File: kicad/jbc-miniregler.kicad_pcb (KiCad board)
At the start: 2 copper layers, 97 x 111 mm, 110 parts, among them J1 Power IN, J2 COM, J3 Lötkolben, Q1 KND3508A, Q2 2N7002, Q3 MMBT3904, Q4 MMBT3904, Q5 ZXMP10A13FTA, SW1 UP, SW2 DOWN, SW3 ENTER, SW4 BACK, SW5 Ein/Aus, U1 OLED-128x32-Module, U2 74LVC1G125, U3 NST175, U4 GS8332-SR, U5 PN7006A, U6 XL7005A, U7 XL7005A, U8 MAX3232

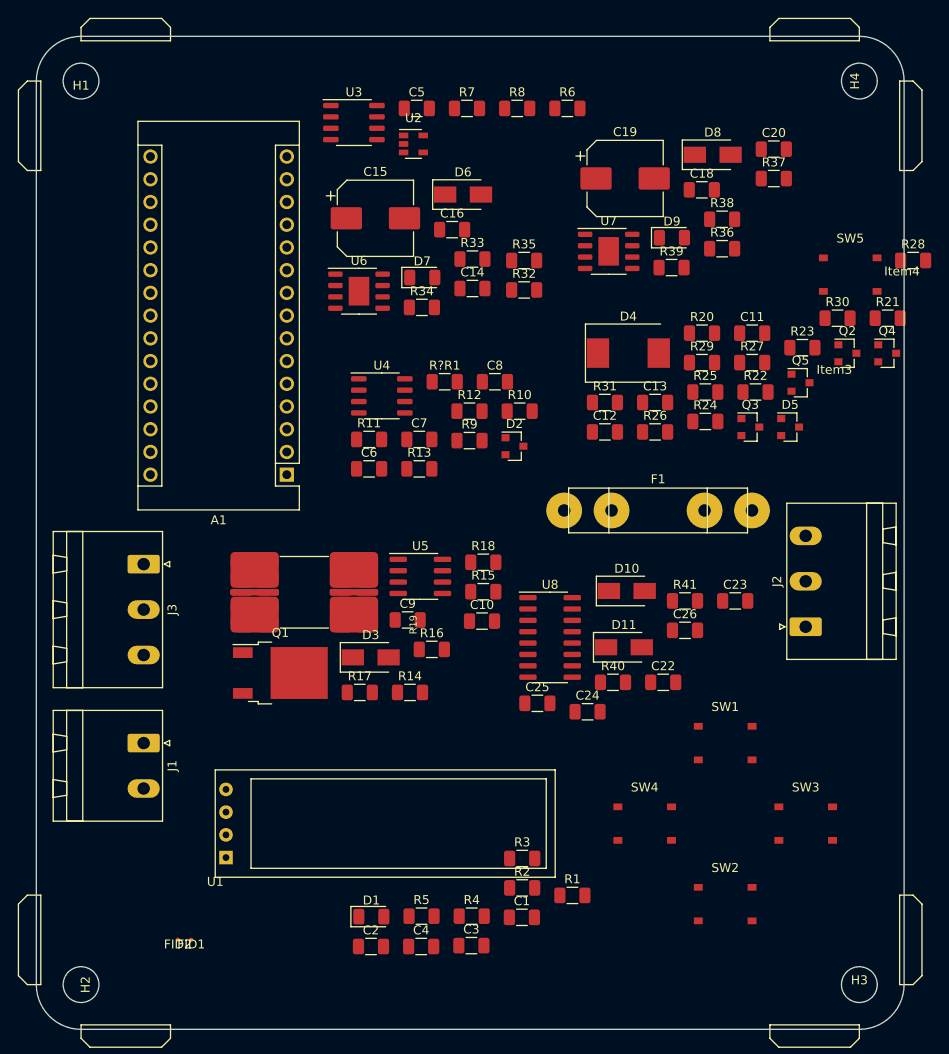
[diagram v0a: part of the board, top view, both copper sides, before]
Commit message: BOM Fertig, 3D auch fast fertig. Ein paar Footrpints fehlen noch.
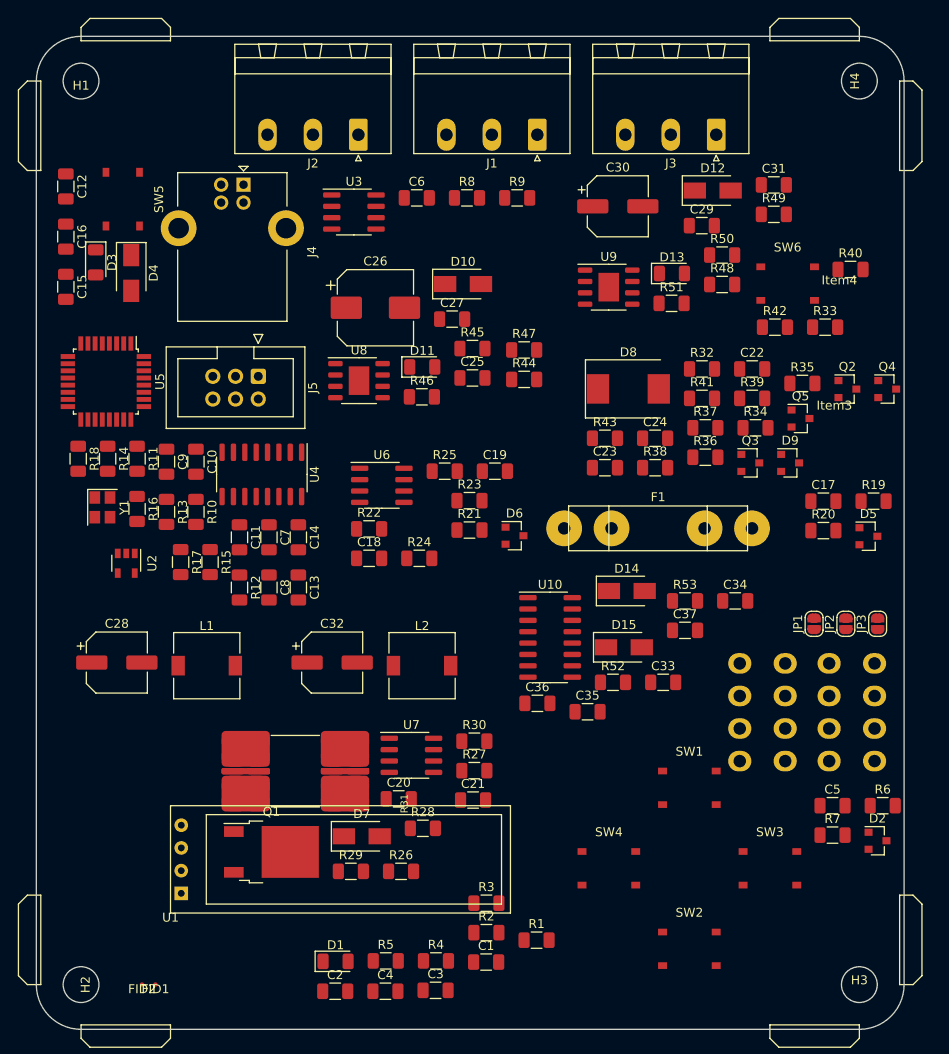
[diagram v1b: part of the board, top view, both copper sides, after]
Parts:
- removed A1: Arduino_Nano_v3.x, Module:Arduino_Nano
- removed the C19 at (103.8, 40.9)
- added C10: 1u, Capacitor_SMD:C_1206_3216Metric, F.Cu at (55.8, 72.5)
- added C11: 100n, Capacitor_SMD:C_1206_3216Metric, F.Cu at (60.7, 81.0)
- added C12: 1u, Capacitor_SMD:C_1206_3216Metric, F.Cu at (41.3, 41.8)
- added C13: 1u, Capacitor_SMD:C_1206_3216Metric, F.Cu at (67.3, 86.6)
- added C14: 100n, Capacitor_SMD:C_1206_3216Metric, F.Cu at (67.3, 81.0)
- added C15: 12p, Capacitor_SMD:C_1206_3216Metric, F.Cu at (41.3, 53.0)
- added C16: 12p, Capacitor_SMD:C_1206_3216Metric, F.Cu at (41.3, 47.4)
- added C17: 100n, Capacitor_SMD:C_1206_3216Metric, F.Cu at (126.0, 77.0)
- added C28: 100u/25V, Capacitor_SMD:CP_Elec_6.3x5.9, F.Cu at (47.0, 95.0)
- added C30: 100u/25V, Capacitor_SMD:CP_Elec_6.3x5.9, F.Cu at (103.0, 44.0)
- added C32: 100u/25V, Capacitor_SMD:CP_Elec_6.3x5.9, F.Cu at (71.1, 95.0)
- added C5: 100n, Capacitor_SMD:C_1206_3216Metric, F.Cu at (127.0, 111.0)
- added C8: 100n, Capacitor_SMD:C_1206_3216Metric, F.Cu at (64.0, 86.6)
- added C9: 100n, Capacitor_SMD:C_1206_3216Metric, F.Cu at (52.5, 72.5)
- added D2: BAV99, Package_TO_SOT_SMD:SOT-23, F.Cu at (132.0, 114.9)
- added D3: grün, LED_SMD:LED_1206_3216Metric, F.Cu at (44.6, 50.3)
- added D4: SS210, Diode_SMD:D_SMA, F.Cu at (48.6, 51.5)
- added D5: BAV99, Package_TO_SOT_SMD:SOT-23, F.Cu at (131.0, 80.9)
- added J10: Makita Minus, htl_connectors:Faston_Tab_6.3mm_vertical, B.Cu at (116.6, 102.4)
- added J11: Bosch Minus, htl_connectors:Faston_Tab_6.3mm_vertical, B.Cu at (126.6, 106.0)
- added J12: ActivEnergy B2-, htl_connectors:Faston_Tab_6.3mm_vertical, B.Cu at (116.6, 98.7)
- added J13: ActivEnergy B1-, htl_connectors:Faston_Tab_6.3mm_vertical, B.Cu at (126.6, 102.4)
- added J4: USB_B, Connector_USB:USB_B_Lumberg_2411_02_Horizontal, F.Cu at (61.2, 41.6)
- added J5: AVR ISP, Connector_IDC:IDC-Header_2x03_P2.54mm_Vertical, F.Cu at (62.8, 63.0)
- added J6: ActivEnergy B2+, htl_connectors:Faston_Tab_6.3mm_vertical, B.Cu at (126.6, 95.1)
- added J7: ActivEnergy B1+, htl_connectors:Faston_Tab_6.3mm_vertical, B.Cu at (126.6, 98.7)
- added J8: Makita Plus, htl_connectors:Faston_Tab_6.3mm_vertical, B.Cu at (116.6, 95.1)
- added J9: Bosch Plus, htl_connectors:Faston_Tab_6.3mm_vertical, B.Cu at (116.6, 106.0)
- added JP1: 20V, Jumper:SolderJumper-2_P1.3mm_Open_RoundedPad1.0x1.5mm, F.Cu at (124.9, 90.7)
- added JP2: 40V, Jumper:SolderJumper-2_P1.3mm_Open_RoundedPad1.0x1.5mm, F.Cu at (128.5, 90.7)
- added JP3: 20V, Jumper:SolderJumper-2_P1.3mm_Open_RoundedPad1.0x1.5mm, F.Cu at (132.0, 90.7)
- added L1: 47u/1A, Inductor_SMD:L_7.3x7.3_H4.5, F.Cu at (57.0, 95.3)
- added L2: 47u/1A, Inductor_SMD:L_7.3x7.3_H4.5, F.Cu at (81.1, 95.3)
- added R11: 1k, Resistor_SMD:R_1206_3216Metric, F.Cu at (49.3, 72.2)
- added R12: 100R, Resistor_SMD:R_1206_3216Metric, F.Cu at (60.7, 86.6)
- added R13: 1k, Resistor_SMD:R_1206_3216Metric, F.Cu at (52.5, 78.2)
- added R14: 100R, Resistor_SMD:R_1206_3216Metric, F.Cu at (46.0, 72.2)
- added R15: 100R, Resistor_SMD:R_1206_3216Metric, F.Cu at (57.4, 83.8)
- added R16: 100R, Resistor_SMD:R_1206_3216Metric, F.Cu at (49.3, 77.8)
- added R17: 1k, Resistor_SMD:R_1206_3216Metric, F.Cu at (54.1, 83.8)
- added R18: 100R, Resistor_SMD:R_1206_3216Metric, F.Cu at (42.7, 72.2)
- added R19: 100k, Resistor_SMD:R_1206_3216Metric, F.Cu at (131.6, 77.0)
- added R20: 1k, Resistor_SMD:R_1206_3216Metric, F.Cu at (126.0, 80.2)
- added R7: 10k, Resistor_SMD:R_1206_3216Metric, F.Cu at (127.0, 114.3)
- added SW5: Reset, htl_smd:SW_Push_5.1mm_H1.5mm, F.Cu at (47.7, 43.2)
- added U4: CH340C, Package_SO:SOIC-16_3.9x9.9mm_P1.27mm, F.Cu at (63.2, 74.0)
- added U5: ATmega328P-AU, Package_QFP:TQFP-32_7x7mm_P0.8mm, F.Cu at (45.8, 63.6)
- added Y1: 16MHz, Crystal:Crystal_SMD_3225-4Pin_3.2x2.5mm, F.Cu at (45.4, 77.7)
- C7: value 10n -> 1u
- Item2: value PCB, 2 Layer, 35um Cu, 1.6mm, TODO size -> PCB, 1 Layer, 35um Cu, 1.6mm, ca. 100x110
- J1: value Power IN -> COM; footprint Connector_Phoenix_MSTB:PhoenixContact_MSTBA_2,5_2-G-5,08_1x02_P5.08mm_Horizontal -> Connector_Phoenix_MSTB:PhoenixContact_MSTBA_2,5_3-G-5,08_1x03_P5.08mm_Horizontal
- U3: footprint Package_SO:SO-8_3.9x4.9mm_P1.27mm -> Package_SO:SOIC-8_3.9x4.9mm_P1.27mm
- U6: renamed from U4; footprint Package_SO:SO-8_3.9x4.9mm_P1.27mm -> Package_SO:SOIC-8_3.9x4.9mm_P1.27mm
- moved R6 85.5 mm to (132.6, 111.0)
- moved J1 81.0 mm to (94.0, 36.0), turned to 180 degrees
- moved J3 80.0 mm to (114.0, 36.0), turned to 180 degrees
- moved J2 74.3 mm to (74.0, 36.0), turned to 180 degrees
- moved U2 56.8 mm to (48.0, 83.9), turned to 270 degrees
- moved R10 37.9 mm to (55.8, 78.2), turned to 270 degrees
- moved C7 20.1 mm to (64.0, 81.0), turned to 270 degrees
- moved C20 20.0 mm to (78.5, 110.2)
- moved C21 20.0 mm to (86.8, 110.4)
- moved D7 20.0 mm to (74.4, 114.4)
- moved Q1 20.0 mm to (64.3, 116.2)
- moved R26 20.0 mm to (78.8, 118.3)
- moved R27 20.0 mm to (87.0, 107.1)
- moved R28 20.0 mm to (81.2, 113.5)
- moved R29 20.0 mm to (73.2, 118.3)
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- renumbered C6 to C18, C8 to C19, C9 to C20, C10 to C21, C11 to C22, C12 to C23, C13 to C24, C14 to C25, C15 to C26, C16 to C27, C18 to C29, C20 to C31, C22 to C33, C23 to C34, C24 to C35, C25 to C36, C26 to C37, C5 to C6, D6 to D10, D7 to D11, D8 to D12, D9 to D13, D10 to D14, D11 to D15, D2 to D6, D3 to D7, D4 to D8, D5 to D9, R9 to R21, R11 to R22, R12 to R23, R13 to R24, R?R1 to R25, R14 to R26, R15 to R27, R16 to R28, R17 to R29, R18 to R30, R19 to R31, R20 to R32, R21 to R33, R22 to R34, R23 to R35, R24 to R36, R25 to R37, R26 to R38, R27 to R39, R28 to R40, R29 to R41, R30 to R42, R31 to R43, R32 to R44, R33 to R45, R34 to R46, R35 to R47, R36 to R48, R37 to R49, R38 to R50, R39 to R51, R40 to R52, R41 to R53, R7 to R8, R8 to R9, SW5 to SW6, U8 to U10, U5 to U7, U6 to U8, U7 to U9
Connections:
- C7 pad 1: Net-(C7-Pad1) -> /Arduino/VUSB
- R10 pad 1: Net-(C7-Pad1) -> /Arduino/VUSB
- R10 pad 2: /Messverstärker/Shunt -> Net-(D3-Pad2)
- R6 pad 1: +5V -> /Arduino/Lötkolbenständer
- R6 pad 2: /Arduino/~RS232-Rx-Enable -> /Arduino/Arduino Nano/A6
- U1 pad 2: (no net) -> +5V
- U2 pad 1: /Arduino/~RS232-Rx-Enable -> /Arduino/VUSB
- U2 pad 4: Net-(A1-Pad2) -> /Arduino/Arduino Nano/D0_RX
- U6 pad 5: Net-(C7-Pad1) -> Net-(C17-Pad2)

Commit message: Reviews und ein paar Verbesserungen
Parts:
- removed J1: COM, Connector_Phoenix_MSTB:PhoenixContact_MSTBA_2,5_3-G-5,08_1x03_P5.08mm_Horizontal
- added C38: 10n, Capacitor_SMD:C_1206_3216Metric, F.Cu at (42.4, 83.1)
- added X1: POWER, htl_connectors:Federklemme_KF142_3P_P5.08mm_C475145, F.Cu at (97.0, 37.6)
- J4: footprint Connector_USB:USB_B_Lumberg_2411_02_Horizontal -> htl_connectors:USB_B_Lumberg_2411_02_Horizontal
- R37: value 100k -> 10k
- X2: renamed from J2; footprint Connector_Phoenix_MSTB:PhoenixContact_MSTBA_2,5_3-G-5,08_1x03_P5.08mm_Horizontal -> htl_connectors:Federklemme_KF142_3P_P5.08mm_C475145
- X3: renamed from J3; footprint Connector_Phoenix_MSTB:PhoenixContact_MSTBA_2,5_3-G-5,08_1x03_P5.08mm_Horizontal -> htl_connectors:Federklemme_KF142_3P_P5.08mm_C475145
- moved C15 17.7 mm to (59.0, 53.7), turned to 0 degrees
- moved C16 13.6 mm to (53.4, 53.7), turned to 0 degrees
- moved C12 13.6 mm to (47.8, 53.7), turned to 0 degrees
- moved D3 11.6 mm to (56.3, 50.4), turned to 0 degrees
- moved D4 10.2 mm to (57.5, 46.4), turned to 0 degrees
- moved J4 8.31 mm to (53.0, 40.0), turned to 90 degrees
- moved SW5 4.42 mm to (49.2, 47.3), turned to 0 degrees
- moved X2 4.32 mm to (78.0, 37.6)
- moved X3 2.57 mm to (116.0, 37.6)

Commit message: Layout
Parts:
- removed H1, H2, H3, H4: MountingHole, htl_mechanical:mountinghole_d4mm_R5mm
- removed J11: Bosch Minus, htl_connectors:Faston_Tab_6.3mm_vertical
- removed J9: Bosch Plus, htl_connectors:Faston_Tab_6.3mm_vertical
- added C39: 100n, Capacitor_SMD:C_1206_3216Metric, F.Cu at (214.5, 33.0)
- added J1: Makita Plus, htl_connectors:Faston_Tab_6.3mm_vertical, B.Cu at (112.5, 112.5)
- added J2: Makita Minus, htl_connectors:Faston_Tab_6.3mm_vertical, B.Cu at (112.5, 73.5)
- added JP4: UART, Jumper:SolderJumper-3_P2.0mm_Open_TrianglePad1.0x1.5mm_NumberLabels, F.Cu at (215.2, 29.6)
- added JP5: UART, Jumper:SolderJumper-3_P2.0mm_Open_TrianglePad1.0x1.5mm_NumberLabels, F.Cu at (223.6, 23.1)
- added JP6: COM, Jumper:SolderJumper-3_P2.0mm_Open_TrianglePad1.0x1.5mm_NumberLabels, F.Cu at (222.2, 29.6)
- added JP7: COM, Jumper:SolderJumper-3_P2.0mm_Open_TrianglePad1.0x1.5mm_NumberLabels, F.Cu at (230.7, 23.1)
- added R54: 3k3, Resistor_SMD:R_1206_3216Metric, F.Cu at (220.1, 33.0)
- added R55: 1k, Resistor_SMD:R_1206_3216Metric, F.Cu at (228.5, 26.5)
- added R56: 1k, Resistor_SMD:R_1206_3216Metric, F.Cu at (228.5, 29.8)
- added R57: 10R, Resistor_SMD:R_1206_3216Metric, F.Cu at (225.7, 33.1)
- added R58: 10R, Resistor_SMD:R_1206_3216Metric, F.Cu at (231.3, 33.1)
- added U11: YD3082EESA, Package_SO:SO-8_3.9x4.9mm_P1.27mm, F.Cu at (215.9, 24.5)
- moved C12 194.6 mm to (232.5, 115.0)
- moved C15 194.6 mm to (243.8, 115.0)
- moved C16 194.6 mm to (238.1, 115.0)
- moved D3 194.6 mm to (241.0, 111.6)
- moved D4 194.6 mm to (242.2, 107.6)
- moved C10 184.8 mm to (240.6, 71.5)
- moved C11 184.8 mm to (245.5, 80.0)
- moved C13 184.8 mm to (252.0, 85.6)
- moved C14 184.8 mm to (252.0, 80.0)
- moved C38 184.8 mm to (227.2, 82.1)
- moved C7 184.8 mm to (248.8, 80.0)
- moved C8 184.8 mm to (248.8, 85.6)
- moved C9 184.8 mm to (237.3, 71.5)
- moved J5 184.8 mm to (247.6, 62.0)
- moved R10 184.8 mm to (240.6, 77.2)
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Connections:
- R52 pad 1: /UART-RS232/RS232_Tx1 -> Net-(D14-Pad1)
- R52 pad 2: Net-(D14-Pad1) -> Net-(R52-Pad2)
- R53 pad 1: /UART-RS232/RS232_Rx1 -> Net-(D15-Pad1)
- R53 pad 2: Net-(D15-Pad1) -> Net-(R53-Pad2)
- U10 pad 11: /Arduino/TxD -> Net-(JP4-Pad3)
- U10 pad 12: /Arduino/RxD -> Net-(JP5-Pad3)
- U10 pad 13: Net-(D15-Pad1) -> Net-(R53-Pad2)
- U10 pad 14: Net-(D14-Pad1) -> Net-(R52-Pad2)
- U5 pad 13: (no net) -> /Arduino/ComDriverEnable
- X2 pad 1: /UART-RS232/RS232_Rx1 -> /UART RS232/RS485/TxD_A
- X2 pad 2: /UART-RS232/RS232_Tx1 -> /UART RS232/RS485/RxD_B
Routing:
- net /Leistungsteil/H+: track 0.00 -> 26.3 mm, vias 0 -> 17
- net GND: track 0.00 -> 21.7 mm, vias 0 -> 7
- net Net-(C21-Pad1): track 0.00 -> 15.0 mm, vias 0 -> 2
- net Net-(Q1-Pad1): track 0.00 -> 14.6 mm, vias 0 -> 2
- net /Leistungsteil/12V: track 0.00 -> 11.4 mm
- net Net-(R27-Pad1): track 0.00 -> 8.70 mm
- net Net-(R29-Pad2): track 0.00 -> 8.65 mm
- net /Messverstärker/Shunt: track 0.00 -> 7.71 mm
- net /Arduino/Heizelement: track 0.00 -> 7.48 mm
- net Net-(R28-Pad1): track 0.00 -> 5.41 mm
- added copper zone on F.Cu, net +BATT
- added copper zone on B.Cu, net /Leistungsteil/H+
- added copper zone on F.Cu, net /Leistungsteil/H+
- added copper zone on F.Cu, net /Leistungsteil/HTC-
- added copper zone on B.Cu, net /Stromversorgung/BAT+
- added copper zone on F.Cu, net /Stromversorgung/BAT+
- added copper zone on B.Cu, net GNDPWR
- added copper zone on F.Cu, net GNDPWR
- added copper zone on F.Cu, net Net-(J12-Pad1)
- added copper zone on F.Cu, net Net-(J7-Pad1)
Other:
- board size 97 x 111 mm -> 110 x 100 mm
- net class 10A added: clearance 0.25, trace_width 10, via_dia 1, via_drill 0.5
- net class Default: clearance 0.25 -> 0.15; trace_width 0.25 -> 0.15
- rule trace_clearance: 0.25 -> 0.15
- rule trace_min: 0.25 -> 0.15
- rule via_min_size: 0.4 -> 0.6

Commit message: wip
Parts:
- added H1: MountingHole, htl_mechanical:mountinghole_d4mm_R5mm, F.Cu at (25.0, 166.8)
- added H2: MountingHole, htl_mechanical:mountinghole_d4mm_R5mm, F.Cu at (25.0, 185.4)
- added H3: MountingHole, htl_mechanical:mountinghole_d4mm_R5mm, F.Cu at (43.6, 166.8)
- added H4: MountingHole, htl_mechanical:mountinghole_d4mm_R5mm, F.Cu at (43.6, 185.4)
- moved D13 99.7 mm to (99.8, 189.8)
- moved R51 93.9 mm to (105.2, 189.7), turned to 180 degrees
- moved C19 93.7 mm to (84.5, 110.4)
- moved R21 93.7 mm to (81.7, 116.9)
- moved R22 93.7 mm to (70.5, 116.8)
- moved R23 93.7 mm to (81.7, 113.7)
- moved R24 93.7 mm to (76.1, 120.1)
- moved R25 93.7 mm to (78.9, 110.4)
- moved U6 93.7 mm to (71.9, 111.9)
- moved C18 93.7 mm to (70.5, 120.1)
- moved D6 93.7 mm to (86.7, 117.6)
- moved R41 85.4 mm to (144.8, 101.8), turned to 90 degrees
- moved R5 76.5 mm to (153.2, 135.2), turned to 270 degrees
- moved D1 76.1 mm to (153.2, 140.1)
- moved R42 60.8 mm to (158.2, 137.2), turned to 180 degrees
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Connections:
- net Net-(C27-Pad2) renamed /Stromversorgung/Spannungsregler 12V/fb
- net Net-(C31-Pad2) renamed /Stromversorgung/Spannungsregler 5V/fb
- net Net-(D10-Pad1) renamed /Stromversorgung/Spannungsregler 12V/sw
- net Net-(D12-Pad1) renamed /Stromversorgung/Spannungsregler 5V/sw
- net Net-(R44-Pad1) renamed /Stromversorgung/Spannungsregler 12V/~en
- net Net-(R48-Pad1) renamed /Stromversorgung/Spannungsregler 5V/~en
- U8 pad 9: (no net) -> GNDPWR
- U9 pad 9: (no net) -> GNDPWR
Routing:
- net /Leistungsteil/12V: track 11.4 -> 33.2 mm, vias 0 -> 2
- net /Stromversorgung/Spannungsregler 12V/fb: track 0.00 -> 15.1 mm, vias 0 -> 2
- net /Stromversorgung/Spannungsregler 5V/fb: track 0.00 -> 15.0 mm, vias 0 -> 2
- net /Stromversorgung/Spannungsregler 12V/~en: track 0.00 -> 12.5 mm, vias 0 -> 2
- net /Stromversorgung/Spannungsregler 5V/~en: track 0.00 -> 12.2 mm, vias 0 -> 2
- net /Arduino/ENTER: track 0.00 -> 11.0 mm
- net /Arduino/UP: track 0.00 -> 10.9 mm
- net /Arduino/DOWN: track 0.00 -> 10.9 mm
- net /Arduino/BACK: track 0.00 -> 10.4 mm
- net /Arduino/Heizelement: track 7.48 -> 14.5 mm
- net /Messverstärker/Shunt: track 7.71 -> 5.50 mm
- net Net-(D1-Pad2): track 0.00 -> 2.05 mm
- net GND: track 21.7 -> 21.4 mm, vias 7 -> 8
- added copper zone on F.Cu, net /Leistungsteil/12V
- added copper zone on F.Cu, net /Stromversorgung/Spannungsregler 12V/IN
- added copper zone on F.Cu, net /Stromversorgung/Spannungsregler 12V/sw
- added copper zone on F.Cu, net /Stromversorgung/Spannungsregler 5V/5V
- added copper zone on F.Cu, net /Stromversorgung/Spannungsregler 5V/IN
- added copper zone on F.Cu, net /Stromversorgung/Spannungsregler 5V/sw

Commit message: WIP Layout, TODO: DRC
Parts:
- D10, D12, D4, D7: footprint Diode_SMD:D_SMA -> htl_smd:D_SMA_wide
- JP1, JP2, JP3: footprint Jumper:SolderJumper-2_P1.3mm_Open_RoundedPad1.0x1.5mm -> htl_smd:SolderJumper-2_2.2x8mm_Open
- L1, L2: footprint Inductor_SMD:L_7.3x7.3_H4.5 -> htl_smd:L_7.3x7.3_H4.5_C216198
- moved Q2 152.3 mm to (108.0, 59.8)
- moved D9 148.3 mm to (115.2, 59.0), turned to 90 degrees
- moved Q4 145.0 mm to (122.8, 59.0)
- moved R33 143.4 mm to (111.8, 59.2), turned to 270 degrees
- moved Q3 142.6 mm to (119.0, 59.0)
- moved R32 141.3 mm to (104.8, 59.2), turned to 90 degrees
- moved R35 139.7 mm to (115.8, 63.5), turned to 180 degrees
- moved R38 138.7 mm to (106.7, 66.6), turned to 270 degrees
- moved R36 134.3 mm to (120.8, 63.5)
- moved D5 130.2 mm to (107.8, 123.2), turned to 90 degrees
- moved R19 128.0 mm to (110.8, 119.2), turned to 270 degrees
- moved R34 125.8 mm to (125.8, 72.5), turned to 90 degrees
- moved R20 122.2 mm to (113.0, 119.2), turned to 270 degrees
- moved C17 120.4 mm to (112.0, 122.8)
- moved D13 117.4 mm to (197.0, 124.0), turned to 270 degrees
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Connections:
- C34 pad 1: GND -> GNDPWR
- C36 pad 1: GND -> GNDPWR
- C37 pad 1: GND -> GNDPWR
- C39 pad 1: GND -> GNDPWR
- D11 pad 1: GNDPWR -> GND
- D13 pad 1: GNDPWR -> GND
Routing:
- net +5V: track 0.00 -> 404.0 mm, vias 0 -> 14
- net /Arduino/Arduino Nano/~RESET: track 0.00 -> 204.3 mm, vias 0 -> 8
- net /Arduino/Strom: track 0.00 -> 196.7 mm, vias 0 -> 6
- net /Arduino/Temperatur: track 0.00 -> 190.8 mm, vias 0 -> 6
- net /Arduino/SCL: track 0.00 -> 153.9 mm, vias 0 -> 2
- net /Arduino/SDA: track 0.00 -> 153.1 mm, vias 0 -> 2
- net /Arduino/BACK: track 10.4 -> 160.7 mm, vias 0 -> 6
- net /Arduino/DOWN: track 10.9 -> 150.5 mm, vias 0 -> 6
- net GND: track 21.4 -> 143.0 mm, vias 8 -> 216
- net /Arduino/Selbsthaltung: track 0.00 -> 114.2 mm, vias 0 -> 4
- net /Arduino/UP: track 10.9 -> 123.0 mm, vias 0 -> 4
- net /Arduino/Ein-Aus-Taster: track 0.00 -> 109.9 mm, vias 0 -> 8
- net /Arduino/ENTER: track 11.0 -> 120.1 mm, vias 0 -> 4
- net /Arduino/Heizelement: track 14.5 -> 111.3 mm, vias 0 -> 6
- net +BATT: track 0.00 -> 86.0 mm, vias 0 -> 1
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- added copper zone on B.Cu, net GND
- added copper zone on F.Cu, net GND

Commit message: DRC clear
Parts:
- moved C20 1.00 mm to (148.2, 136.8)
- moved C28 0.75 mm to (152.2, 127.0)
- moved C30 0.75 mm to (159.8, 131.8)
- moved C32 0.75 mm to (182.0, 131.0)
- moved D7 0.75 mm to (147.2, 140.2)
- moved R26 0.75 mm to (148.2, 134.5)
- moved R27 0.75 mm to (148.2, 132.0)
- moved R42 0.75 mm to (158.2, 138.0)
- moved R44 0.75 mm to (157.5, 122.2)
- moved R46 0.75 mm to (152.5, 122.2)
- moved R50 0.75 mm to (177.2, 130.8)
- moved C38 0.25 mm to (184.8, 104.8)
- moved D10 0.25 mm to (152.5, 118.8)
- moved D12 0.25 mm to (173.8, 130.8)
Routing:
- net /Arduino/UP: track 123.0 -> 121.6 mm
- net GND: track 143.0 -> 142.3 mm, vias 216 -> 213
- net /Arduino/Heizelement: track 111.3 -> 112.0 mm
